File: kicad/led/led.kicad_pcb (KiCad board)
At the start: 2 copper layers, 73 x 25.1 mm, 45 parts, among them J1 Conn_01x06, J2 Conn_01x09_Male, U1 LF353DR, U2 LF353DR, U3 LF353DR, U4 LM339DR, U5 LM339DR

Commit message: Maybe finished LED board I think
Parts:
- removed C1, C10, C11, C12, C2, C3, C4, C5, C6, C7, C8, C9: 100n, Capacitor_SMD:C_1206_3216Metric
- removed RV1, RV3, RV4: 10k, Potentiometer_THT:Potentiometer_Runtron_RM-065_Vertical
- removed U1, U2, U3: LF353DR, Package_SO:SOIC-8_3.9x4.9mm_P1.27mm
- removed U4, U5: LM339DR, Package_SO:SO-14_3.9x8.65mm_P1.27mm
- added D1: ORANGE, LED_SMD:LED_1210_3225Metric, F.Cu at (45.2, 46.4)
- added D10: YELLOW, LED_SMD:LED_1210_3225Metric, F.Cu at (62.7, 55.9)
- added D11: GREEN, LED_SMD:LED_1210_3225Metric, F.Cu at (62.7, 65.4)
- added D12: BLUE, LED_SMD:LED_1210_3225Metric, F.Cu at (62.7, 74.9)
- added D13: ORANGE, LED_SMD:LED_1210_3225Metric, F.Cu at (71.8, 46.4)
- added D14: YELLOW, LED_SMD:LED_1210_3225Metric, F.Cu at (71.8, 55.9)
- added D15: GREEN, LED_SMD:LED_1210_3225Metric, F.Cu at (71.8, 65.4)
- added D16: BLUE, LED_SMD:LED_1210_3225Metric, F.Cu at (71.8, 74.9)
- added D17: ORANGE, LED_SMD:LED_1210_3225Metric, F.Cu at (80.6, 46.4)
- added D18: YELLOW, LED_SMD:LED_1210_3225Metric, F.Cu at (80.6, 55.9)
- added D19: GREEN, LED_SMD:LED_1210_3225Metric, F.Cu at (80.6, 65.4)
- added D2: YELLOW, LED_SMD:LED_1210_3225Metric, F.Cu at (45.2, 55.9)
- added D20: BLUE, LED_SMD:LED_1210_3225Metric, F.Cu at (80.6, 74.9)
- added D21: ORANGE, LED_SMD:LED_1210_3225Metric, F.Cu at (105.4, 46.4)
- added D22: YELLOW, LED_SMD:LED_1210_3225Metric, F.Cu at (105.4, 55.9)
- added D23: GREEN, LED_SMD:LED_1210_3225Metric, F.Cu at (105.4, 65.4)
- added D24: BLUE, LED_SMD:LED_1210_3225Metric, F.Cu at (105.4, 74.9)
- added D25: ORANGE, LED_SMD:LED_1210_3225Metric, F.Cu at (114.3, 46.4)
- added D26: YELLOW, LED_SMD:LED_1210_3225Metric, F.Cu at (114.3, 55.9)
- added D27: GREEN, LED_SMD:LED_1210_3225Metric, F.Cu at (114.3, 65.4)
- added D28: BLUE, LED_SMD:LED_1210_3225Metric, F.Cu at (114.3, 74.9)
- added D29: ORANGE, LED_SMD:LED_1210_3225Metric, F.Cu at (123.2, 46.4)
- added D3: GREEN, LED_SMD:LED_1210_3225Metric, F.Cu at (45.2, 65.4)
- added D30: YELLOW, LED_SMD:LED_1210_3225Metric, F.Cu at (123.2, 55.9)
- added D31: GREEN, LED_SMD:LED_1210_3225Metric, F.Cu at (123.1, 65.4)
- added D32: BLUE, LED_SMD:LED_1210_3225Metric, F.Cu at (123.2, 74.9)
- added D33: ORANGE, LED_SMD:LED_1210_3225Metric, F.Cu at (132.1, 46.4)
- added D34: YELLOW, LED_SMD:LED_1210_3225Metric, F.Cu at (132.1, 55.9)
- added D35: GREEN, LED_SMD:LED_1210_3225Metric, F.Cu at (132.1, 65.4)
- added D36: BLUE, LED_SMD:LED_1210_3225Metric, F.Cu at (132.1, 74.9)
- added D37: ORANGE, LED_SMD:LED_1210_3225Metric, F.Cu at (141.0, 46.4)
- added D38: YELLOW, LED_SMD:LED_1210_3225Metric, F.Cu at (141.0, 55.9)
- added D39: GREEN, LED_SMD:LED_1210_3225Metric, F.Cu at (141.0, 65.4)
- added D4: BLUE, LED_SMD:LED_1210_3225Metric, F.Cu at (45.2, 74.9)
- added D40: BLUE, LED_SMD:LED_1210_3225Metric, F.Cu at (141.0, 74.9)
- added D5: ORANGE, LED_SMD:LED_1210_3225Metric, F.Cu at (54.0, 46.4)
- added D6: YELLOW, LED_SMD:LED_1210_3225Metric, F.Cu at (54.0, 55.9)
- added D7: GREEN, LED_SMD:LED_1210_3225Metric, F.Cu at (54.0, 65.4)
- added D8: BLUE, LED_SMD:LED_1210_3225Metric, F.Cu at (54.0, 74.9)
- added D9: ORANGE, LED_SMD:LED_1210_3225Metric, F.Cu at (62.7, 46.4)
- added J10: Conn_01x04_Male, Connector_PinHeader_2.54mm:PinHeader_1x04_P2.54mm_Horizontal, B.Cu at (151.1, 106.0)
- added J100: Conn_01x01_Male, Connector_PinSocket_2.54mm:PinSocket_1x01_P2.54mm_Vertical, F.Cu at (106.7, 113.0)
- added J3: Conn_01x04_Male, Connector_PinHeader_2.54mm:PinHeader_1x04_P2.54mm_Horizontal, B.Cu at (66.7, 105.9)
- added J4: Conn_01x04_Male, Connector_PinHeader_2.54mm:PinHeader_1x04_P2.54mm_Horizontal, B.Cu at (78.7, 105.9)
- added J5: Conn_01x04_Male, Connector_PinHeader_2.54mm:PinHeader_1x04_P2.54mm_Horizontal, B.Cu at (90.8, 106.0)
- added J6: Conn_01x04_Male, Connector_PinHeader_2.54mm:PinHeader_1x04_P2.54mm_Horizontal, B.Cu at (102.9, 106.0)
- added J7: Conn_01x04_Male, Connector_PinHeader_2.54mm:PinHeader_1x04_P2.54mm_Horizontal, B.Cu at (114.9, 106.0)
- added J8: Conn_01x04_Male, Connector_PinHeader_2.54mm:PinHeader_1x04_P2.54mm_Horizontal, B.Cu at (127.0, 106.0)
- added J9: Conn_01x04_Male, Connector_PinHeader_2.54mm:PinHeader_1x04_P2.54mm_Horizontal, B.Cu at (139.1, 105.9)
- added R19: R, Resistor_SMD:R_1206_3216Metric, F.Cu at (80.6, 69.8)
- added R20: R, Resistor_SMD:R_1206_3216Metric, F.Cu at (80.6, 79.4)
- added R21: R, Resistor_SMD:R_1206_3216Metric, F.Cu at (105.4, 50.8)
- added R22: R, Resistor_SMD:R_1206_3216Metric, F.Cu at (105.4, 60.3)
- added R23: R, Resistor_SMD:R_1206_3216Metric, F.Cu at (105.4, 69.8)
- added R24: R, Resistor_SMD:R_1206_3216Metric, F.Cu at (105.4, 79.4)
- added R25: R, Resistor_SMD:R_1206_3216Metric, F.Cu at (114.3, 50.8)
- added R26: R, Resistor_SMD:R_1206_3216Metric, F.Cu at (114.3, 60.3)
- added R27: R, Resistor_SMD:R_1206_3216Metric, F.Cu at (114.3, 69.8)
- added R37: R, Resistor_SMD:R_1206_3216Metric, F.Cu at (141.0, 50.8)
- added R38: R, Resistor_SMD:R_1206_3216Metric, F.Cu at (141.0, 60.3)
- added R39: R, Resistor_SMD:R_1206_3216Metric, F.Cu at (141.0, 69.8)
- added R40: R, Resistor_SMD:R_1206_3216Metric, F.Cu at (141.0, 79.4)
- added R6: R, Resistor_SMD:R_1206_3216Metric, F.Cu at (54.0, 60.3)
- added R7: R, Resistor_SMD:R_1206_3216Metric, F.Cu at (54.0, 69.8)
- added R8: R, Resistor_SMD:R_1206_3216Metric, F.Cu at (54.0, 79.4)
- added R9: R, Resistor_SMD:R_1206_3216Metric, F.Cu at (62.7, 50.8)
- J1: value Conn_01x06 -> Conn_01x04_Male; footprint Connector_PinHeader_2.54mm:PinHeader_1x06_P2.54mm_Horizontal -> Connector_PinHeader_2.54mm:PinHeader_1x04_P2.54mm_Horizontal; moved to B.Cu
- J2: value Conn_01x09_Male -> Conn_01x04_Male; footprint Connector_PinHeader_2.54mm:PinHeader_1x09_P2.54mm_Horizontal -> Connector_PinHeader_2.54mm:PinHeader_1x04_P2.54mm_Horizontal; moved to B.Cu
- R1, R2, R3, R4, R5: value 100k -> R
- R10, R11, R12, R28, R29, R30: value 137 -> R
- R13, R14, R15, R31, R32, R33: value 931 -> R
- R16, R17, R18, R34, R35, R36: value 1k87 -> R
- moved J2 137.4 mm to (54.6, 105.9), turned to 90 degrees
- moved R1 126.3 mm to (45.1, 50.8), turned to 180 degrees
- moved R4 123.3 mm to (45.1, 79.4)
- moved R3 121.6 mm to (45.3, 69.8), turned to 0 degrees
- moved R2 121.5 mm to (45.1, 60.3), turned to 0 degrees
- moved R5 120.0 mm to (54.0, 50.8), turned to 180 degrees
- moved R12 100.5 mm to (62.7, 79.4), turned to 0 degrees
- moved R11 88.4 mm to (62.7, 69.8), turned to 0 degrees
- moved R15 84.6 mm to (71.8, 69.8)
- moved J1 82.6 mm to (42.5, 105.9), turned to 90 degrees
- moved R18 78.5 mm to (80.6, 60.3), turned to 0 degrees
- moved R10 77.3 mm to (62.7, 60.3), turned to 0 degrees
- moved R14 73.1 mm to (71.8, 60.3)
- moved R17 68.8 mm to (80.6, 50.8), turned to 180 degrees
- moved R16 65.1 mm to (71.8, 79.4), turned to 0 degrees
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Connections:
- J1 pad 3: +5V -> Net-(D2-Pad1)
- J1 pad 4: +15V -> Net-(J1-Pad4)
- R1 pad 2: Net-(R1-Pad2) -> +5V
- R10 pad 1: Net-(C4-Pad1) -> +5V
- R10 pad 2: Net-(R10-Pad2) -> Net-(D10-Pad2)
- R11 pad 1: Net-(C5-Pad1) -> +5V
- R11 pad 2: Net-(R11-Pad2) -> Net-(D11-Pad2)
- R12 pad 1: Net-(C6-Pad1) -> +5V
- R13 pad 1: audio_left -> Net-(D13-Pad2)
- R13 pad 2: Net-(C4-Pad1) -> +5V
- R14 pad 1: Net-(R10-Pad2) -> +5V
- R14 pad 2: Net-(C5-Pad1) -> Net-(D14-Pad2)
- R15 pad 1: Net-(R11-Pad2) -> +5V
- R15 pad 2: Net-(C6-Pad1) -> Net-(D15-Pad2)
- R16 pad 1: Net-(C1-Pad2) -> +5V
- R16 pad 2: GND -> Net-(D16-Pad2)
- R17 pad 2: GND -> +5V
- R18 pad 1: Net-(C3-Pad2) -> +5V
- R18 pad 2: GND -> Net-(D18-Pad2)
- R2 pad 1: Net-(R1-Pad2) -> +5V
- R2 pad 2: Net-(R2-Pad2) -> Net-(D2-Pad2)
- R28 pad 1: Net-(C10-Pad1) -> +5V
- R28 pad 2: Net-(R28-Pad2) -> Net-(D28-Pad2)
- R29 pad 1: Net-(C11-Pad1) -> Net-(D29-Pad2)
- R29 pad 2: Net-(R29-Pad2) -> +5V
- R3 pad 1: Net-(R2-Pad2) -> +5V
- R3 pad 2: Net-(R3-Pad2) -> Net-(D3-Pad2)
- R30 pad 1: Net-(C12-Pad1) -> +5V
- R31 pad 1: audio_right -> +5V
- R31 pad 2: Net-(C10-Pad1) -> Net-(D31-Pad2)
- R32 pad 1: Net-(R28-Pad2) -> +5V
- R32 pad 2: Net-(C11-Pad1) -> Net-(D32-Pad2)
- R33 pad 1: Net-(R29-Pad2) -> Net-(D33-Pad2)
- R33 pad 2: Net-(C12-Pad1) -> +5V
- R34 pad 1: Net-(C7-Pad2) -> +5V
- R34 pad 2: GND -> Net-(D34-Pad2)
- R35 pad 1: Net-(C8-Pad2) -> +5V
- R35 pad 2: GND -> Net-(D35-Pad2)
- R36 pad 1: Net-(C9-Pad2) -> +5V
- R36 pad 2: GND -> Net-(D36-Pad2)
- R4 pad 1: Net-(R3-Pad2) -> +5V
- R4 pad 2: Net-(R4-Pad2) -> Net-(D4-Pad2)
- R5 pad 1: Net-(R4-Pad2) -> Net-(D5-Pad2)
- R5 pad 2: GND -> +5V
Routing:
- net +5V: track 98.4 -> 0.00 mm, vias 2 -> 0
- net Net-(D17-Pad1): track 0.00 -> 65.5 mm
- net Net-(D21-Pad1): track 0.00 -> 65.4 mm
- net Net-(D13-Pad1): track 0.00 -> 64.1 mm
- net Net-(D25-Pad1): track 0.00 -> 64.1 mm
- net Net-(J1-Pad4): track 0.00 -> 63.9 mm
- net Net-(D37-Pad1): track 0.00 -> 63.9 mm
- net Net-(D9-Pad1): track 0.00 -> 62.8 mm
- net Net-(D29-Pad1): track 0.00 -> 62.8 mm
- net Net-(D33-Pad1): track 0.00 -> 62.5 mm
- net Net-(D5-Pad1): track 5.21 -> 62.5 mm
- net Net-(D18-Pad1): track 0.00 -> 56.3 mm
- net Net-(D22-Pad1): track 0.00 -> 56.2 mm
- net Net-(D14-Pad1): track 0.00 -> 54.9 mm
- net Net-(D26-Pad1): track 0.00 -> 54.9 mm
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- added copper zone on F.Cu, net +5V
- removed copper zone on B.Cu, net GND
- removed copper zone on F.Cu, net GND
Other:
- board size 73 x 25.1 mm -> 123.8 x 82.5 mm

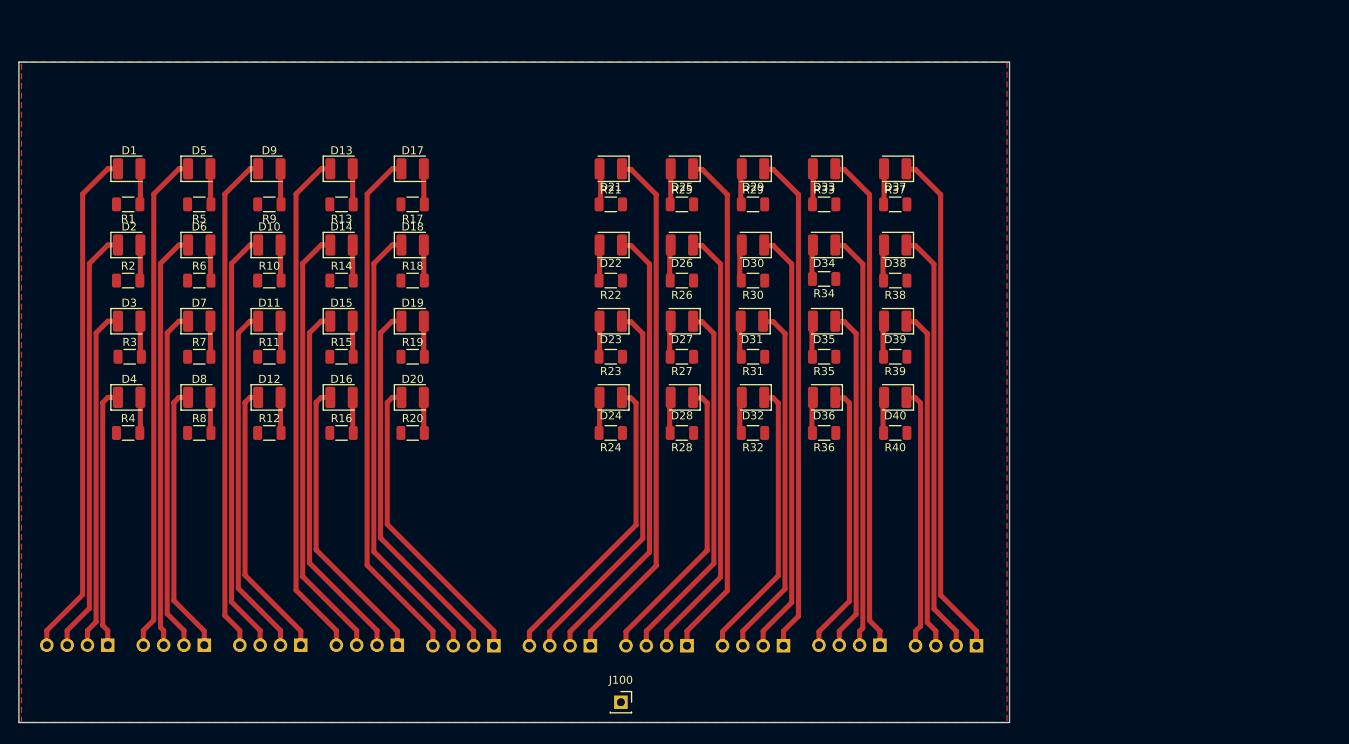
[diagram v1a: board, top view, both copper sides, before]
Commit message: Copied LED board, and made new revision with full connectors, not split
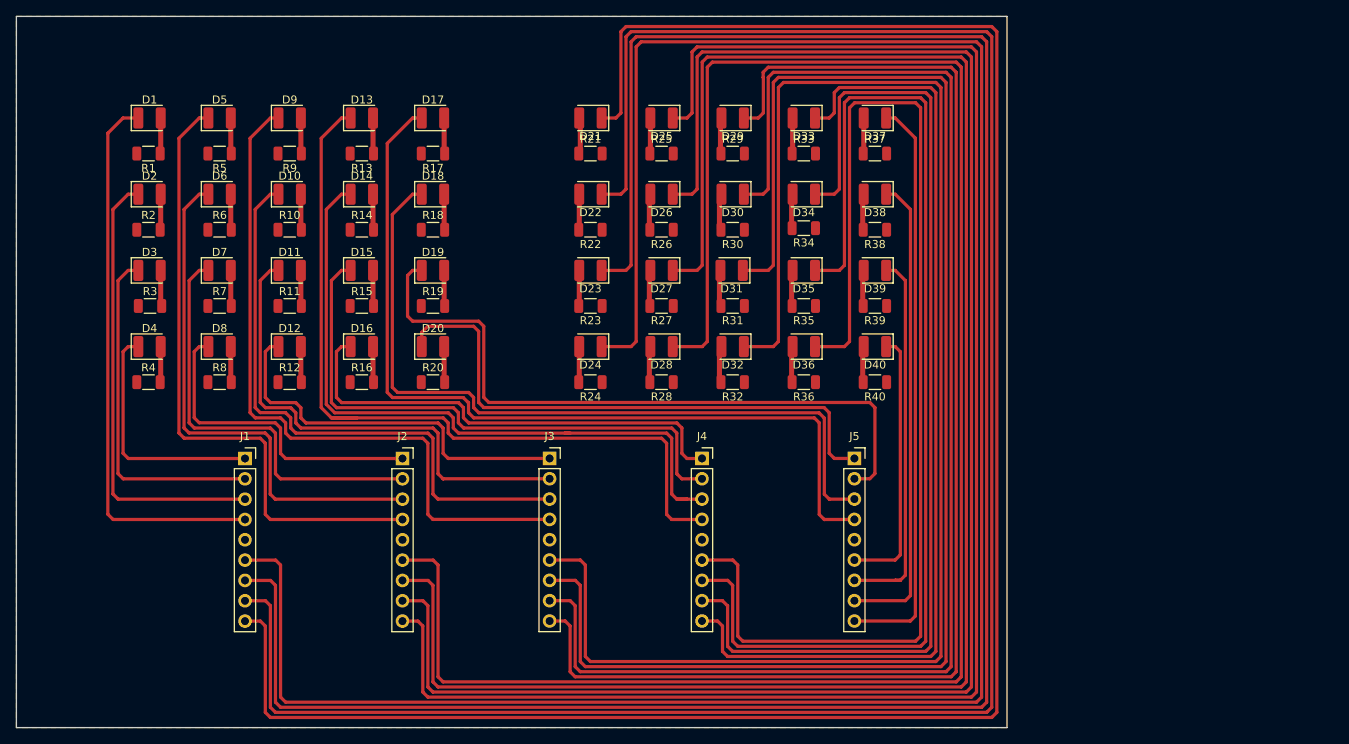
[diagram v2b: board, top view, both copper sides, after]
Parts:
- removed J10, J6, J7, J8, J9: Conn_01x04_Male, Connector_PinHeader_2.54mm:PinHeader_1x04_P2.54mm_Horizontal
- removed J100: Conn_01x01_Male, Connector_PinSocket_2.54mm:PinSocket_1x01_P2.54mm_Vertical
- J1, J2, J3, J4, J5: value Conn_01x04_Male -> Conn_01x09_Male; footprint Connector_PinHeader_2.54mm:PinHeader_1x04_P2.54mm_Horizontal -> Connector_PinSocket_2.54mm:PinSocket_1x09_P2.54mm_Vertical; moved to F.Cu
- moved J5 50.8 mm to (135.9, 82.6), turned to 0 degrees
- moved J4 44.7 mm to (116.8, 82.6), turned to 0 degrees
- moved J3 38.9 mm to (97.8, 82.6), turned to 0 degrees
- moved J2 34.0 mm to (79.4, 82.6), turned to 0 degrees
- moved J1 29.0 mm to (59.7, 82.6), turned to 0 degrees
- moved D36 6.84 mm to (129.5, 68.6)
- moved D12 6.84 mm to (65.3, 68.6)
- moved D16 6.84 mm to (74.3, 68.6)
- moved D20 6.84 mm to (83.2, 68.6)
- moved D34 6.84 mm to (129.5, 49.5)
- moved D35 6.84 mm to (129.5, 59.1)
- moved R34 6.84 mm to (129.5, 53.8)
- moved D4 6.84 mm to (47.8, 68.6)
- moved D8 6.84 mm to (56.5, 68.6)
- moved D24 6.84 mm to (102.9, 68.6)
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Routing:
- net Net-(D24-Pad1): track 37.9 -> 275.8 mm
- net Net-(D23-Pad1): track 47.1 -> 267.5 mm
- net Net-(D22-Pad1): track 56.2 -> 259.2 mm
- net Net-(D28-Pad1): track 36.6 -> 231.9 mm
- net Net-(D21-Pad1): track 65.4 -> 251.0 mm
- net Net-(D27-Pad1): track 45.7 -> 223.7 mm
- net Net-(D26-Pad1): track 54.9 -> 215.4 mm
- net Net-(D32-Pad1): track 35.3 -> 189.4 mm
- net Net-(D25-Pad1): track 64.1 -> 207.2 mm
- net Net-(D31-Pad1): track 44.4 -> 181.3 mm
- net Net-(D30-Pad1): track 53.6 -> 172.9 mm
- net Net-(D36-Pad1): track 33.9 -> 146.2 mm
- net Net-(D29-Pad1): track 62.8 -> 164.7 mm
- net Net-(D35-Pad1): track 43.1 -> 138.0 mm
- net Net-(D34-Pad1): track 52.2 -> 129.7 mm
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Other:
- board size 123.8 x 82.5 mm -> 123.8 x 88.9 mm

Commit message: Made some PCBs
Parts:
- moved J2 0.64 mm to (78.7, 82.5)
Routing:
- net Net-(D21-Pad1): track 251.0 -> 152.9 mm
- net Net-(D22-Pad1): track 259.2 -> 176.7 mm
- net Net-(D23-Pad1): track 267.5 -> 195.1 mm
- net Net-(D24-Pad1): track 275.8 -> 213.5 mm
- net Net-(D28-Pad1): track 231.9 -> 256.7 mm
- net Net-(D27-Pad1): track 223.7 -> 238.3 mm
- net Net-(D25-Pad1): track 207.2 -> 196.1 mm
- net Net-(D26-Pad1): track 215.4 -> 219.9 mm
- net Net-(D35-Pad1): track 138.0 -> 140.5 mm
- net Net-(D30-Pad1): track 172.9 -> 175.5 mm
- net Net-(D29-Pad1): track 164.7 -> 167.2 mm
- net Net-(D36-Pad1): track 146.2 -> 148.8 mm
- net Net-(D33-Pad1): track 121.5 -> 124.0 mm
- net Net-(D32-Pad1): track 189.4 -> 192.0 mm
- net Net-(D31-Pad1): track 181.3 -> 183.8 mm
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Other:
- board size 123.8 x 88.9 mm -> 114.9 x 82.5 mm
